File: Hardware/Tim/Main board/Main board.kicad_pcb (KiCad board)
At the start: 4 copper layers, 113 x 66 mm, 179 parts, among them J1 SOICbite, J10 Conn_01x03_Socket, J11 Nichrome, J12 USB_C_Receptacle_USB2.0, J13 Conn_01x02_Socket, J14 Conn_01x02_Pin, J15 Conn_01x04_Socket, J16 Conn_01x02_Pin, J2 USB_C_Receptacle_USB2.0, J3 Conn_01x04_Socket, J4 Conn_01x04_Socket, J5 Conn_01x04_Socket, J6 Conn_01x02_Socket, J7 Conn_01x02_Socket, J8 U.FL, J9 SOICbite, Q1 IRLML0060TRPBF, Q2 IRLML0060TRPBF, U1 RP2040, U10 MAX-M10S, U11 ADP7105ACPZ-5.0-R7, U12 ADP7105ACPZ-3.3-R7, U13 ADP7105ACPZ-5.0-R7, U14 TPS2121RUXR, U15 TPS2121RUXR, U2 W25Q64JVZP, U3 MS5607-02BA, U4 BMI270, U5 ADP7105ACPZ-3.3-R7, U6 DRF1262TL, U7 RP2040, U8 W25Q64JVZP, U9 LT3120JV-PBF, Y1 445I23D12M00000, Y3 445I23D12M00000

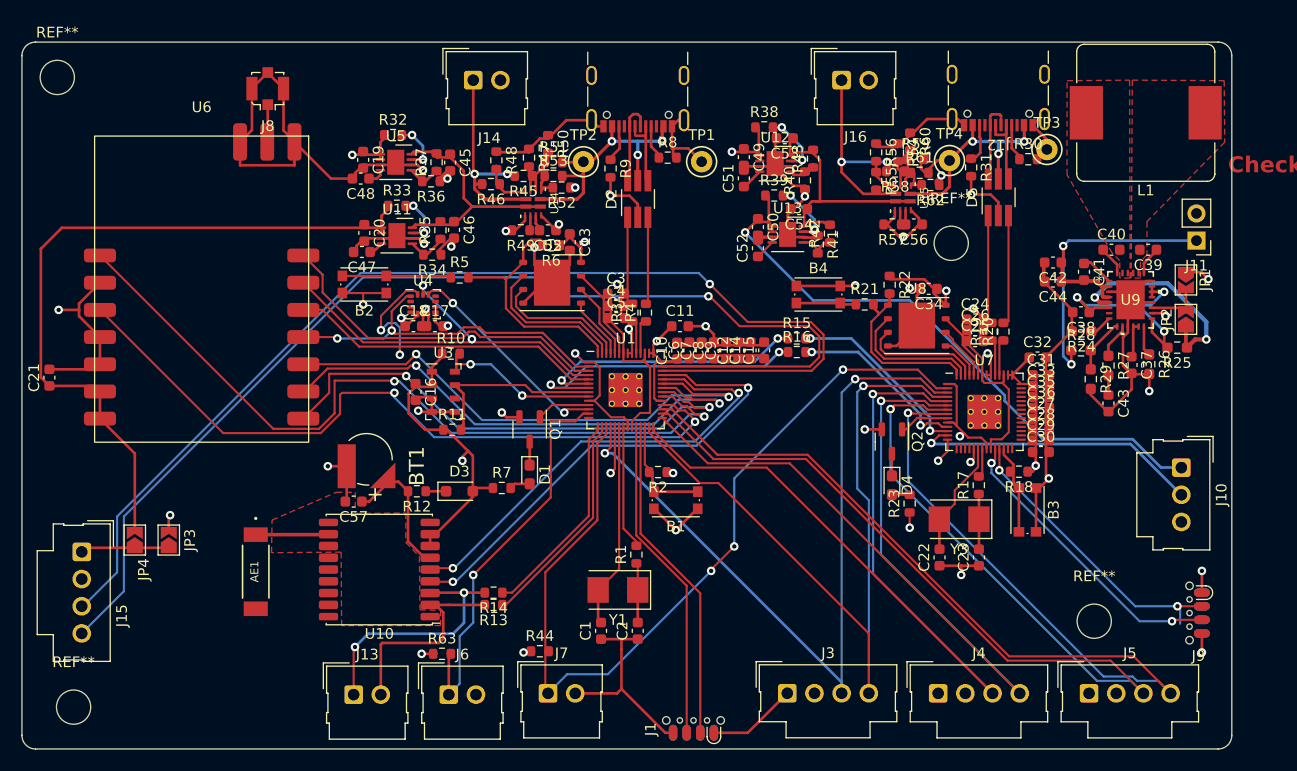
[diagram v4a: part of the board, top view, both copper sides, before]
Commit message: fixed the drc things that are problems
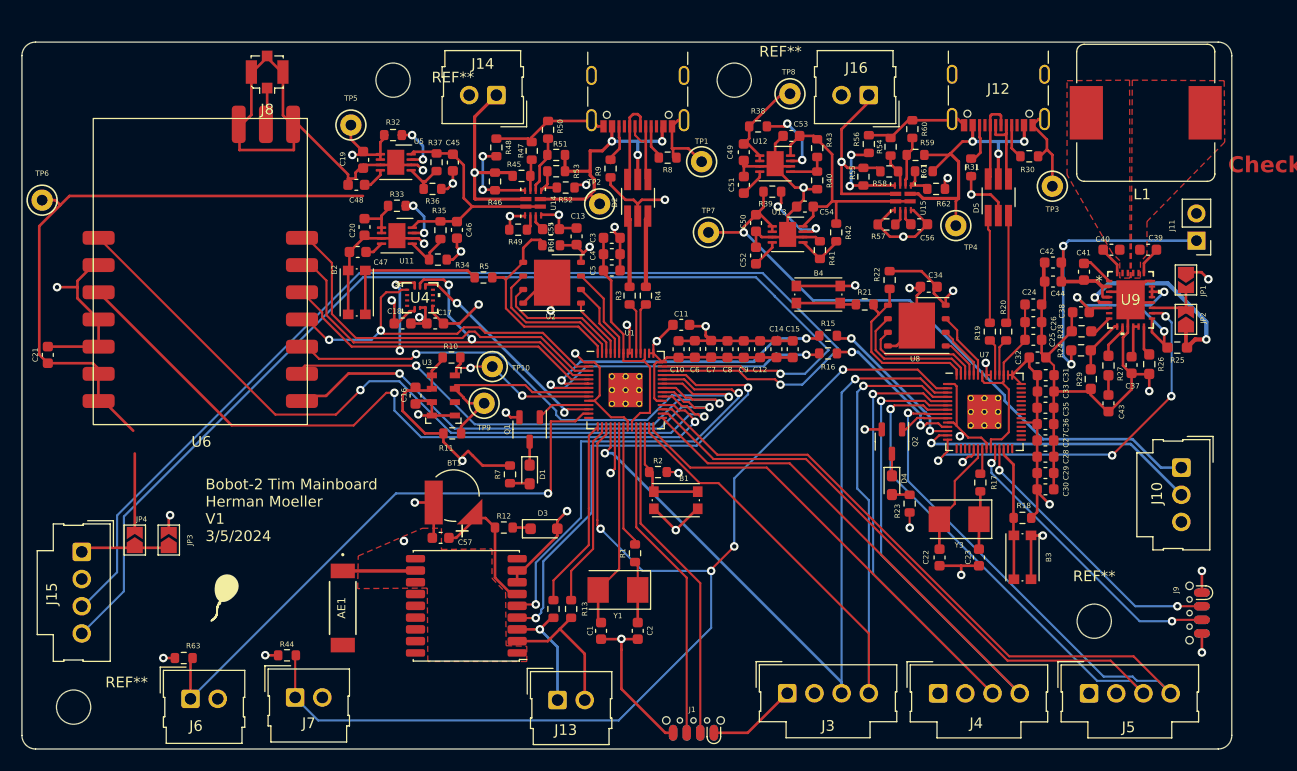
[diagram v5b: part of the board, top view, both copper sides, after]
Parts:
- added REF**: BalloonArt, BPPlib:BalloonArt, F.Cu at (76.1, 105.3)
- added TP10: TestPoint, TestPoint:TestPoint_Keystone_5000-5004_Miniature, F.Cu at (101.1, 83.7)
- added TP5: TestPoint, TestPoint:TestPoint_Keystone_5000-5004_Miniature, F.Cu at (87.9, 61.1)
- added TP6: TestPoint, TestPoint:TestPoint_Keystone_5000-5004_Miniature, F.Cu at (59.0, 68.1)
- added TP7: TestPoint, TestPoint:TestPoint_Keystone_5000-5004_Miniature, F.Cu at (121.3, 71.1)
- added TP8: TestPoint, TestPoint:TestPoint_Keystone_5000-5004_Miniature, F.Cu at (128.9, 58.2)
- added TP9: TestPoint, TestPoint:TestPoint_Keystone_5000-5004_Miniature, F.Cu at (100.3, 87.1)
- U4: footprint Package_LGA:LGA-14_3x2.5mm_P0.5mm_LayoutBorder3x4y -> BPPlib:BMI270_BOS-L
- moved REF** 31.4 mm to (91.8, 56.9)
- moved REF** 25.4 mm to (123.7, 56.9)
- moved J6 24.1 mm to (72.9, 114.7)
- moved R63 24.1 mm to (72.3, 110.9)
- moved J7 23.6 mm to (82.7, 114.6)
- moved R44 23.6 mm to (81.9, 110.6)
- moved J13 19.1 mm to (107.2, 114.8)
- moved AE1 8.81 mm to (87.1, 106.2)
- moved BT1 8.81 mm to (97.5, 95.7)
- moved C57 8.81 mm to (96.3, 99.7)
- moved R12 8.81 mm to (102.2, 98.7)
- moved U10 8.81 mm to (98.7, 106.0)
- moved D3 8.64 mm to (105.9, 98.8)
- moved R13 7.26 mm to (108.5, 106.3), turned to -90 degrees
- moved TP4 6.11 mm to (144.4, 70.5)
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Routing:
- net /CUT: track 3.73 -> 35.8 mm, vias 2 -> 4
- net /LS1: track 81.7 -> 109.3 mm, vias 3 -> 4
- net +3V3: track 141.0 -> 162.5 mm
- net /LS2: track 37.4 -> 55.7 mm
- net GND: track 314.8 -> 328.7 mm
- net Net-(J13-Pin_1): track 24.0 -> 11.1 mm, vias 2 -> 1
- net Net-(J13-Pin_2): track 20.1 -> 13.5 mm
- net +5V: track 124.6 -> 130.9 mm
- net VCC: track 24.9 -> 30.7 mm
- net Net-(U1-VREG_VOUT): track 17.2 -> 22.6 mm
- net Net-(U15-PR1): track 3.79 -> 8.92 mm, vias 0 -> 2
- net /SPI0_SCK: track 38.3 -> 42.9 mm
- net Net-(U7-RUN): track 8.30 -> 12.5 mm
- net Net-(B2-Pad2): track 10.6 -> 14.6 mm
- net Net-(U14-PR1): track 4.76 -> 8.40 mm, vias 0 -> 2
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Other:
- board text added: "Bobot-2 Tim Mainboard Herman Moeller V1 3/5/2024"

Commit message: minor changes
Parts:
- moved D3 16.0 mm to (90.0, 98.3), turned to 90 degrees
- moved BT1 15.3 mm to (86.9, 106.7), turned to 0 degrees
- moved AE1 14.9 mm to (97.4, 117.1), turned to 0 degrees
- moved R12 12.8 mm to (89.8, 102.0), turned to -90 degrees
- moved R13 9.96 mm to (109.5, 96.4)
- moved R14 9.96 mm to (107.8, 96.4)
- moved C57 9.92 mm to (90.8, 107.9), turned to -90 degrees
- moved REF** 4.40 mm to (79.2, 102.2)
- moved U10 1.58 mm to (97.2, 105.5), turned to -90 degrees
- moved L1 0.76 mm to (162.1, 60.7)
- moved U6 0.45 mm to (73.8, 75.2)
- moved J8 0.40 mm to (79.9, 56.5)
- moved J14 0.25 mm to (101.5, 58.5)
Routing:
- net Net-(J13-Pin_1): track 11.1 -> 28.3 mm, vias 1 -> 0
- net Net-(J13-Pin_2): track 13.5 -> 29.9 mm, vias 0 -> 2
- net /GPS_RX: track 17.9 -> 7.58 mm
- net /GPS_TX: track 17.4 -> 7.13 mm
- net +5V: track 130.9 -> 135.3 mm
- net /LS1: track 109.3 -> 106.2 mm
- net /TIMEPULSE: track 45.7 -> 42.9 mm
- net /LS2: track 55.7 -> 53.9 mm
- net /SPI0_SCK: track 42.9 -> 41.8 mm
- net /EXTINT: track 43.3 -> 42.2 mm
- net /SPI0_CS_RAD: track 35.4 -> 34.5 mm
- net GND: track 328.7 -> 327.9 mm
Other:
- board size 113 x 66 mm -> 113 x 65.5 mm
- board text added: "Bobot-2 Tim Mainboard Herman Moeller V1 3/7/2024"
- board text removed: "Bobot-2 Tim Mainboard Herman Moeller V1 3/5/2024"
- board text removed: "Check if these need to be size matched"

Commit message: Update changes hopefully good
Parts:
- removed C37: 4.7uF, Capacitor_SMD:C_0603_1608Metric
- removed C38: 10uF, Capacitor_SMD:C_0603_1608Metric
- removed C39, C40: 220nF, Capacitor_SMD:C_0603_1608Metric
- removed C41: 22nF, Capacitor_SMD:C_0603_1608Metric
- removed C42, C44: 22uF, Capacitor_SMD:C_0603_1608Metric
- removed C43: 680p, Capacitor_SMD:C_0603_1608Metric
- removed JP1: SolderJumper_2_Open, Jumper:SolderJumper-2_P1.3mm_Open_TrianglePad1.0x1.5mm
- removed L1: 3.3uH, BPPlib:L_Bourns_SRP1265A
- removed R24: 81.1k, Resistor_SMD:R_0603_1608Metric_Pad0.98x0.95mm_HandSolder
- removed R25: 5m, Resistor_SMD:R_0603_1608Metric_Pad0.98x0.95mm_HandSolder
- removed R26: 75k, Resistor_SMD:R_0603_1608Metric_Pad0.98x0.95mm_HandSolder
- removed R27: 56.2k, Resistor_SMD:R_0603_1608Metric_Pad0.98x0.95mm_HandSolder
- removed R28, R29: 154k, Resistor_SMD:R_0603_1608Metric_Pad0.98x0.95mm_HandSolder
- removed U9: LT3120JV-PBF, BPPlib:LQFN28_Rev0_ADI
- removed Y3: 445I23D12M00000, Crystal:Crystal_SMD_5032-2Pin_5.0x3.2mm
- added 0.3_Ohm_Resistor1: 03, Package_TO_SOT_SMD:TO-263-2, F.Cu at (161.5, 60.3)
- added C58: 100nF, Capacitor_SMD:C_0603_1608Metric, F.Cu at (92.9, 96.3)
- added C59: 1uF, Capacitor_SMD:C_0603_1608Metric, F.Cu at (95.4, 96.3)
- added J17: Conn_01x04_Pin, Connector_Molex:Molex_SL_171971-0004_1x04_P2.54mm_Vertical, F.Cu at (173.4, 97.2)
- added J18: Conn_01x03_Socket, Connector_Molex:Molex_SL_171971-0003_1x03_P2.54mm_Vertical, F.Cu at (62.2, 95.5)
- added LM1084-ADJ1: LM1084-ADJ, Package_TO_SOT_SMD:TO-263-3_TabPin2, F.Cu at (161.2, 82.1)
- added MOSFET2: IRF540N, Package_TO_SOT_SMD:TO-252-2, F.Cu at (173.2, 60.2)
- added Y2: 12MHz, Crystal:Crystal_SMD_2520-4Pin_2.5x2.0mm, F.Cu at (113.7, 104.7)
- C1, C2, C22, C23: value 22pF -> 10pF
- J11: value Nichrome -> Conn_01x02_Pin; footprint Connector_PinHeader_2.54mm:PinHeader_1x02_P2.54mm_Vertical -> Connector_Molex:Molex_SL_171971-0002_1x02_P2.54mm_Vertical
- J8: footprint Connector_Coaxial:U.FL_Molex_MCRF_73412-0110_Vertical -> Connector_Coaxial:SMA_Amphenol_132289_EdgeMount
- JP2: value SolderJumper_2_Open -> SolderJumper_2_Bridged; footprint Jumper:SolderJumper-2_P1.3mm_Open_TrianglePad1.0x1.5mm -> Jumper:SolderJumper-2_P1.3mm_Bridged_Pad1.0x1.5mm
- Y1: value 445I23D12M00000 -> 12MHz; footprint Crystal:Crystal_SMD_5032-2Pin_5.0x3.2mm -> Crystal:Crystal_SMD_2520-4Pin_2.5x2.0mm
- moved Y1 32.8 mm to (144.9, 97.9)
- moved C15 20.6 mm to (113.5, 95.5), turned to -90 degrees
- moved C14 20.1 mm to (107.6, 81.2), turned to 180 degrees
- moved REF** 18.1 mm to (73.9, 101.9)
- moved J10 17.4 mm to (173.2, 108.7), turned to 90 degrees
- moved C29 14.9 mm to (141.2, 84.2), turned to 180 degrees
- moved J9 12.9 mm to (172.0, 119.0), turned to 0 degrees
- moved JP2 12.0 mm to (170.9, 68.3)
- moved J11 8.26 mm to (174.7, 74.4), turned to -90 degrees
- moved JP3 8.09 mm to (68.9, 107.7), turned to 0 degrees
- moved J15 7.49 mm to (62.7, 108.5)
- moved C30 4.94 mm to (148.2, 97.0), turned to -90 degrees
- moved JP4 4.83 mm to (68.3, 104.6)
- moved R3 1.09 mm to (114.0, 78.1)
- moved R4 1.09 mm to (115.6, 78.1)
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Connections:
- C27 pad 1: +3V3 -> +3V3_R
- C28 pad 1: +3V3 -> +3V3_R
- C29 pad 1: +3V3 -> +3V3_R
- C30 pad 1: +3V3 -> +3V3_R
- C31 pad 1: +3V3 -> +3V3_R
- C32 pad 1: +3V3 -> +3V3_R
- C33 pad 1: +3V3 -> +3V3_R
- C34 pad 1: +3V3 -> +3V3_R
- C35 pad 1: +3V3 -> +3V3_R
- C36 pad 1: +3V3 -> +3V3_R
- C49 pad 1: +3V3 -> +3V3_R
- C50 pad 1: +5V -> +5V_R
- J10 pad 1: +5V -> +5V_R
- J11 pad 2: GND -> Net-(J11-Pin_2)
- J16 pad 1: Net-(J16-Pin_1) -> +BATT
- J9 pad 1: +3V3 -> +3V3_R
- JP2 pad 1: +BATT -> /CUT
- R18 pad 1: +3V3 -> +3V3_R
- R22 pad 1: +3V3 -> +3V3_R
- R23 pad 1: +3V3 -> +3V3_R
- R38 pad 1: +3V3 -> +3V3_R
- R39 pad 1: +5V -> +5V_R
- R55 pad 2: Net-(J16-Pin_1) -> +BATT
- R58 pad 2: Net-(J16-Pin_1) -> +BATT
- TP7 pad 1: +5V -> +5V_R
- TP8 pad 1: +3V3 -> +3V3_R
- U12 pad 1: +3V3 -> +3V3_R
- U12 pad 2: +3V3 -> +3V3_R
- U13 pad 1: +5V -> +5V_R
- U13 pad 2: +5V -> +5V_R
- U15 pad 7: Net-(J16-Pin_1) -> +BATT
- U7 pad 1: +3V3 -> +3V3_R
- U7 pad 10: +3V3 -> +3V3_R
- U7 pad 22: +3V3 -> +3V3_R
- U7 pad 33: +3V3 -> +3V3_R
- U7 pad 42: +3V3 -> +3V3_R
- U7 pad 43: +3V3 -> +3V3_R
- U7 pad 44: +3V3 -> +3V3_R
- U7 pad 48: +3V3 -> +3V3_R
- U7 pad 49: +3V3 -> +3V3_R
- U8 pad 8: +3V3 -> +3V3_R
- Y1 pad 1: Net-(C2-Pad2) -> Net-(C23-Pad2)
- Y1 pad 2: Net-(U1-XIN) -> GND
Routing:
- net +5V_R: track 0.00 -> 87.0 mm, vias 0 -> 1
- net +3V3_R: track 0.00 -> 63.4 mm, vias 0 -> 6
- net +5V: track 135.3 -> 81.5 mm, vias 1 -> 0
- net /PWM_MC: track 0.00 -> 52.3 mm, vias 0 -> 3
- net +BATT: track 19.7 -> 49.4 mm, vias 2 -> 1
- net Net-(LM1084-ADJ1-VO): track 0.00 -> 29.1 mm
- net /CUT: track 35.8 -> 62.6 mm, vias 4 -> 3
- net Net-(U9-ISN): track 23.2 -> 0.00 mm, vias 3 -> 0
- net Net-(J11-Pin_1): track 34.8 -> 14.0 mm, vias 2 -> 0
- net Net-(J11-Pin_2): track 0.00 -> 20.5 mm
- net Net-(J16-Pin_1): track 20.2 -> 0.00 mm, vias 1 -> 0
- net /SWD_R: track 26.2 -> 39.2 mm
- net +3V3: track 162.5 -> 149.8 mm, vias 20 -> 13
- net /PWM_EMRG_REL: track 27.3 -> 39.4 mm
- net /SWCLK_R: track 27.9 -> 38.3 mm
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- added copper zone on In2.Cu, net +3V3_R
- removed copper zone on F.Cu, net Net-(C39-Pad2)
- removed copper zone on F.Cu, net Net-(C40-Pad2)
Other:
- board size 113 x 65.5 mm -> 120.9 x 66.6 mm
- board text added: "Bobot-2 Tim Mainboard Herman Moeller V1 4/17/2024"
- board text removed: "Bobot-2 Tim Mainboard Herman Moeller V1 3/7/2024"

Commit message: Updated things
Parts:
- added C37: 1uF, Capacitor_SMD:C_0603_1608Metric, F.Cu at (106.4, 57.9)
- added C38: 100nF, Capacitor_SMD:C_0603_1608Metric, F.Cu at (108.2, 57.9)
- added C39: 1uF, Capacitor_SMD:C_0603_1608Metric, F.Cu at (106.4, 53.8)
- added C40: 100nF, Capacitor_SMD:C_0603_1608Metric, F.Cu at (106.4, 55.4)
- added C41: 1uF, Capacitor_SMD:C_0603_1608Metric, F.Cu at (140.2, 57.9)
- added C42: 100nF, Capacitor_SMD:C_0603_1608Metric, F.Cu at (141.7, 57.9)
- added C43: 1uF, Capacitor_SMD:C_0603_1608Metric, F.Cu at (141.0, 53.8)
- added C44: 100nF, Capacitor_SMD:C_0603_1608Metric, F.Cu at (141.0, 55.5)
- moved C28 14.1 mm to (145.7, 79.9), turned to 90 degrees
- moved REF** 1.28 mm to (74.0, 103.1)
- moved J1 0.25 mm to (119.9, 118.9)
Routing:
- net GND: track 320.1 -> 335.8 mm, vias 40 -> 41
- net /STEP: track 115.4 -> 107.7 mm, vias 1 -> 6
- net VCC: track 30.7 -> 38.1 mm, vias 3 -> 5
- net VBUS: track 28.0 -> 35.1 mm, vias 3 -> 5
- net Net-(J14-Pin_1): track 18.7 -> 25.8 mm
- net +BATT: track 49.4 -> 56.1 mm
- net /DIR: track 115.1 -> 110.2 mm, vias 1 -> 6
- net /LS1: track 105.9 -> 109.6 mm
- net +3V3_R: track 63.4 -> 66.7 mm
- net +3V3: track 149.8 -> 150.4 mm
